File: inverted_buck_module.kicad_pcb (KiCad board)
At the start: 2 copper layers, 11 parts, among them J1 Conn_01x03, U1 TPS63710

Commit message: more wip
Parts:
- removed Cin1: 2x22uF 16V, Capacitor_SMD:C_0603_1608Metric
- removed Cout1: 2 x 22uF10V / 0805, Capacitor_SMD:C_0805_2012Metric
- removed Cx1: 2.2uF 16V 0603, Capacitor_SMD:C_0603_1608Metric
- removed R1: 130k, Resistor_SMD:R_0603_1608Metric
- removed R2: 24k, Resistor_SMD:R_0603_1608Metric
- added Ccp2: 10uF 16V, Capacitor_SMD:C_0805_2012Metric, F.Cu at (110.7, 61.8)
- added Ccp3: 10uF 16V, Capacitor_SMD:C_0805_2012Metric, F.Cu at (110.7, 59.8)
- added Cin: 22uF 16V, Capacitor_SMD:C_1206_3216Metric, F.Cu at (116.0, 56.5)
- added Cin2: 22uF 16V, Capacitor_SMD:C_1206_3216Metric, F.Cu at (118.5, 56.5)
- added Cin3: 22uF 16V, Capacitor_SMD:C_1206_3216Metric, F.Cu at (121.0, 56.5)
- added Cinx: 2.2uF 16V, Capacitor_SMD:C_0603_1608Metric, F.Cu at (114.0, 56.3)
- added Cout: 47uF 6.3V, Capacitor_SMD:C_0805_2012Metric, F.Cu at (102.7, 56.6)
- added Cout2: 47uF 6.3V, Capacitor_SMD:C_0805_2012Metric, F.Cu at (105.0, 56.5)
- added Cout3: 47uF 6.3V, Capacitor_SMD:C_0805_2012Metric, F.Cu at (107.5, 56.5)
- added Rfbb1: 24kΩ, Resistor_SMD:R_0402_1005Metric, F.Cu at (110.0, 52.0)
- added Rfbt1: 130kΩ, Resistor_SMD:R_0402_1005Metric, F.Cu at (110.0, 53.0)
- Caux: renamed from Caux1; value 220nF -> 220nF 10V
- Ccap1: value 1uF -> 1uF 10V
- Ccp: renamed from Ccp1; value 3 x 10uF 16V / 0805 -> 10uF 16V
- L1: value 4.7 uH -> 4.7uH; footprint Inductor_SMD:L_0603_1608Metric -> Inductor_SMD:L_Coilcraft_LPS4018
- moved L1 46.1 mm to (106.4, 60.6), turned to 180 degrees
- moved U1 45.1 mm to (110.7, 56.6), turned to -90 degrees
- moved J1 38.9 mm to (121.1, 65.0), turned to -90 degrees
- moved Ccap1 37.5 mm to (106.5, 52.3), turned to 90 degrees
- moved Caux 27.9 mm to (114.0, 52.3), turned to 90 degrees
- moved Ccp 26.4 mm to (110.7, 63.8), turned to 180 degrees
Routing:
- net GND: track 0.00 -> 39.1 mm, vias 0 -> 1
- net Vout: track 0.00 -> 35.5 mm
- net Vin: track 0.00 -> 21.7 mm, vias 0 -> 2
- net Net-(U1-SW): track 0.00 -> 7.80 mm
- net Net-(U1-CP): track 0.00 -> 5.89 mm
- net Net-(U1-CAP): track 0.00 -> 3.85 mm
- net Net-(U1-FB): track 0.00 -> 3.35 mm
- net Net-(U1-VAUX): track 0.00 -> 2.93 mm
- net Net-(U1-VREF): track 0.00 -> 2.16 mm
- added copper zone on B.Cu, net GND
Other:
- board outline added: 23 x 17.5 mm

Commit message: layout tweaks
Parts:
- moved Cin3 3.49 mm to (118.0, 54.7)
- moved Cin2 2.98 mm to (118.0, 59.5), turned to -90 degrees
- moved Caux 2.97 mm to (113.5, 55.2), turned to -90 degrees
- moved Cin 2.97 mm to (115.5, 59.5), turned to -90 degrees
- moved Cinx 2.48 mm to (113.5, 58.7), turned to -90 degrees
- moved Ccap1 1.02 mm to (107.5, 52.5), turned to 180 degrees
- moved Cout3 0.89 mm to (107.2, 55.7)
- moved Cout 0.88 mm to (102.8, 55.7)
- moved Ccp 0.84 mm to (110.8, 63.0)
- moved Cout2 0.83 mm to (105.0, 55.7)
- moved Ccp2 0.82 mm to (110.8, 61.0)
- moved Rfbt1 0.80 mm to (110.0, 52.2)
- moved Rfbb1 0.80 mm to (110.0, 51.2)
- moved Ccp3 0.79 mm to (110.8, 59.0)
- moved U1 0.78 mm to (110.7, 55.8)
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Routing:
- net GND: track 39.1 -> 16.3 mm, vias 1 -> 14
- net Vin: track 21.7 -> 27.2 mm, vias 2 -> 0
- net Net-(U1-VAUX): track 2.93 -> 1.55 mm
- net Net-(U1-CAP): track 3.85 -> 2.64 mm
- net Vout: track 35.5 -> 36.1 mm
- added copper zone on F.Cu, net GND
- added copper zone on F.Cu, net Vout

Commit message: fill areas
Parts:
- removed Ccap1: 1uF 10V, Capacitor_SMD:C_0603_1608Metric
- removed Rfbb1: 24kΩ, Resistor_SMD:R_0402_1005Metric
- removed Rfbt1: 130kΩ, Resistor_SMD:R_0402_1005Metric
- added Ccap: 1uF 10V, Capacitor_SMD:C_0603_1608Metric, F.Cu at (107.5, 52.5)
- added Rfbb: 24kΩ, Resistor_SMD:R_0402_1005Metric, F.Cu at (110.0, 51.5)
- added Rfbt: 130kΩ, Resistor_SMD:R_0402_1005Metric, F.Cu at (110.0, 52.5)
- J1: footprint Connector_PinHeader_2.54mm:PinHeader_1x03_P2.54mm_Horizontal -> Connector_PinHeader_2.54mm:PinHeader_1x03_P2.54mm_Vertical
- moved J1 1.58 mm to (119.5, 65.0)
- moved Cout 0.25 mm to (103.0, 55.7)
- moved Caux 0.20 mm to (113.5, 55.0)
- moved Cinx 0.20 mm to (113.5, 58.5)
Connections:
- net Net-(U1-CP) renamed /CP
- net Net-(U1-SW) renamed /SW
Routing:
- net GND: track 16.3 -> 14.1 mm
- net Vin: track 27.2 -> 29.2 mm
- net Vout: track 36.1 -> 35.4 mm
- added copper zone on F.Cu, net /CP
- added copper zone on F.Cu, net /SW
- added copper zone on F.Cu, net Vin
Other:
- board size 23 x 17.5 mm -> 21 x 17 mm

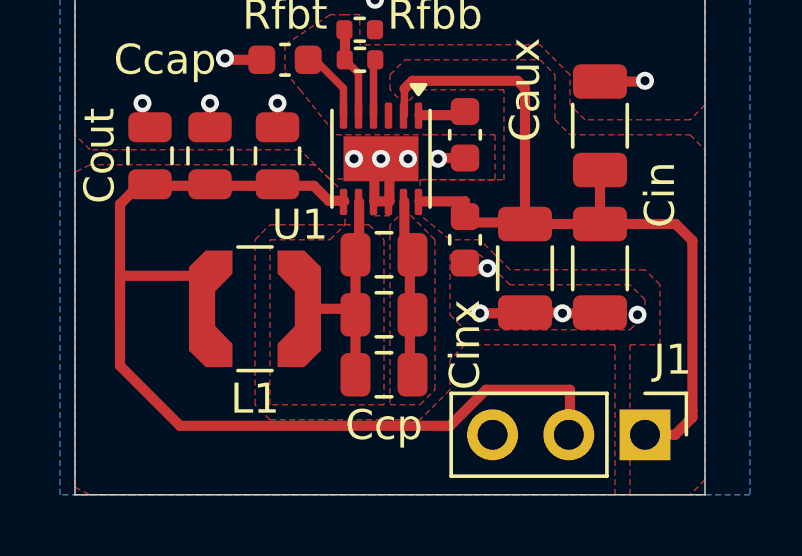
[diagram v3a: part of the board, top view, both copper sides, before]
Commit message: vout tweak
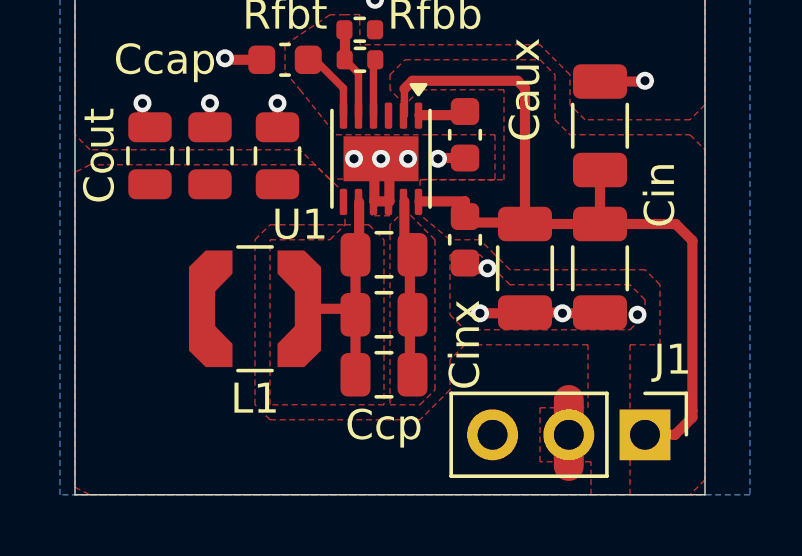
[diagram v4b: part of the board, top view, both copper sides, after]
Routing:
- net Vout: track 35.4 -> 2.26 mm
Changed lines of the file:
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@@
 	)
 	(segment
-		(start 114.2 63.5)
-		(end 117 63.5)
-		(width 0.34)
-		(layer "F.Cu")
-		(net 4)
-	)
-	(segment
-		(start 104.734998 59.7)
-		(end 104.735 59.700002)
-		(width 0.34)
-		(layer "F.Cu")
-		(net 4)
-	)
-	(segment
-		(start 113 64.7)
-		(end 114.2 63.5)
-		(width 0.34)
-		(layer "F.Cu")
-		(net 4)
-	)
-	(segment
-		(start 102.659598 56.7)
-		(end 102.636997 56.677399)
-		(width 0.34)
-		(layer "F.Cu")
-		(net 4)
-	)
-	(segment
-		(start 109.459623 57.2)
-		(end 108.959623 57.2)
-		(width 0.34)
-		(layer "F.Cu")
-		(net 4)
-	)
-	(segment
-		(start 109.480315 57.220692)
-		(end 109.459623 57.2)
-		(width 0.34)
-		(layer "F.Cu")
-		(net 4)
-	)
-	(segment
-		(start 102.636997 56.677399)
-		(end 102 57.314396)
-		(width 0.34)
-		(layer "F.Cu")
-		(net 4)
-	)
-	(segment
-		(start 108.459623 56.7)
-		(end 102.659598 56.7)
-		(width 0.34)
-		(layer "F.Cu")
-		(net 4)
-	)
-	(segment
-		(start 102 61.2)
-		(end 102 62.7)
-		(width 0.34)
-		(layer "F.Cu")
-		(net 4)
-	)
-	(segment
-		(start 108.959623 57.2)
-		(end 108.459623 56.7)
-		(width 0.34)
-		(layer "F.Cu")
-		(net 4)
-	)
-	(segment
-		(start 102 62.7)
-		(end 104 64.7)
-		(width 0.34)
-		(layer "F.Cu")
-		(net 4)
-	)
-	(segment
-		(start 102 61.2)
-		(end 102 59.7)
-		(width 0.34)
-		(layer "F.Cu")
-		(net 4)
-	)
-	(segment
-		(start 117 63.5)
-		(end 117 65)
-		(width 0.34)
-		(layer "F.Cu")
-		(net 4)
-	)
-	(segment
-		(start 102 59.7)
-		(end 104.734998 59.7)
-		(width 0.34)
-		(layer "F.Cu")
-		(net 4)
-	)
-	(segment
-		(start 104 64.7)
-		(end 113 64.7)
-		(width 0.34)
-		(layer "F.Cu")
-		(net 4)
-	)
-	(segment
-		(start 102 57.314396)
-		(end 102 61.2)
-		(width 0.34)
-		(layer "F.Cu")
-		(net 4)
-	)
-	(segment
-		(start 104.735 59.700002)
-		(end 104.735 59.7)
-		(width 0.34)
+		(start 116.96 65)
+		(end 116.96 63.84)
+		(width 1)
+		(layer "F.Cu")
+		(net 4)
+	)
+	(segment
+		(start 116.96 63.84)
+		(end 117 63.8)
+		(width 0.34)
+		(layer "F.Cu")
+		(net 4)
+	)
+	(segment
+		(start 116.96 65)
+		(end 116.96 66.04)
+		(width 1)
 		(layer "F.Cu")
 		(net 4)
@@
 		(polygon
 			(pts
-				(xy 106.5 58.5) (xy 107 58) (xy 109.5 58) (xy 109.5 58) (xy 109.5 56.975) (xy 109 56.475) (xy 108.5 56)
-				(xy 101 56) (xy 100.5 56.25) (xy 100.5 66.75) (xy 101 67) (xy 118.5 67) (xy 118.5 62) (xy 113.5 62)
-				(xy 113 62.5) (xy 113 63.5) (xy 112 64.5) (xy 107 64.5) (xy 106.5 64)
+				(xy 106.5 58.5) (xy 107 58) (xy 109.5 58) (xy 109.5 56.975) (xy 109 56.475) (xy 108.5 56) (xy 101 56)
+				(xy 100.5 56.25) (xy 100.5 66.75) (xy 101 67) (xy 117.7 67) (xy 117.7 65.9) (xy 116 65.9) (xy 116 64.1)
+				(xy 117.6 64.1) (xy 117.6 62) (xy 113.5 62) (xy 113 62.5) (xy 113 63.5) (xy 112 64.5) (xy 107 64.5)
+				(xy 106.5 64)
 			)
 		)

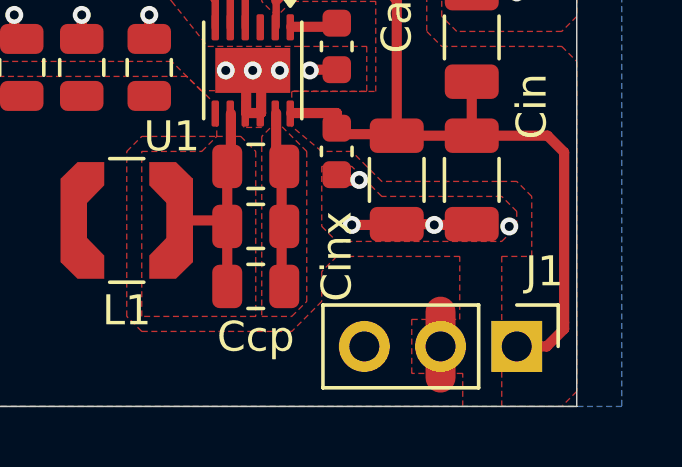
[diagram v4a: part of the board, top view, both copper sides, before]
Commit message: flip connector to the backside
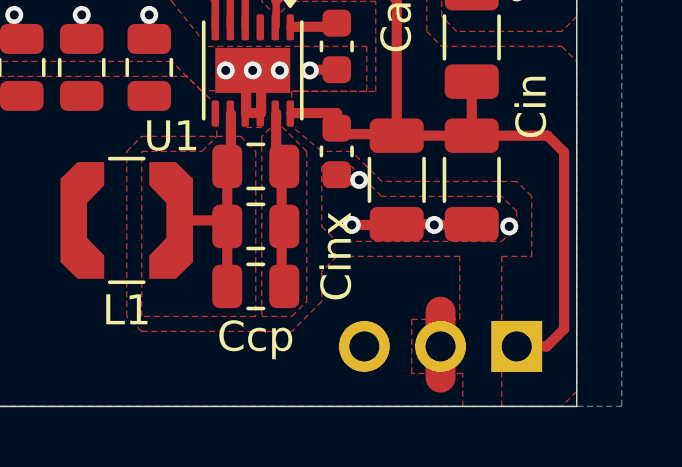
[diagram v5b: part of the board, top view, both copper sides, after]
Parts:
- J1: moved to B.Cu
- turned J1 to 90 degrees

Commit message: revert prop refs
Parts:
- renumbered Caux to Caux1, Ccap to Ccap1, Ccp to Ccp1, Cin to Cin1, Cinx to Cinx1, Cout to Cout1, Rfbb to Rfbb1, Rfbt to Rfbt1
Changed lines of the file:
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@@
 		(descr "Capacitor SMD 1206 (3216 Metric), square (rectangular) end terminal, IPC-7351 nominal, (Body size source: IPC-SM-782 page 76, https://www.pcb-3d.com/wordpress/wp-content/uploads/ipc-sm-782a_amendment_1_and_2.pdf), generated with kicad-footprint-generator")
 		(tags "capacitor")
-		(property "Reference" "Cin"
+		(property "Reference" "Cin1"
 			(at -2.45 -4.5 90)
 			(layer "F.SilkS")
@@
 		(descr "Capacitor SMD 0603 (1608 Metric), square (rectangular) end terminal, IPC-7351 nominal, (Body size source: IPC-SM-782 page 76, https://www.pcb-3d.com/wordpress/wp-content/uploads/ipc-sm-782a_amendment_1_and_2.pdf), generated with kicad-footprint-generator")
 		(tags "capacitor")
-		(property "Reference" "Ccap"
+		(property "Reference" "Ccap1"
 			(at 4 0 0)
 			(layer "F.SilkS")
@@
 		(descr "Resistor SMD 0402 (1005 Metric), square (rectangular) end terminal, IPC-7351 nominal, (Body size source: IPC-SM-782 page 72, https://www.pcb-3d.com/wordpress/wp-content/uploads/ipc-sm-782a_amendment_1_and_2.pdf), generated with kicad-footprint-generator")
 		(tags "resistor")
-		(property "Reference" "Rfbt"
+		(property "Reference" "Rfbt1"
 			(at 2.5 1.5 0)
 			(layer "F.SilkS")
@@
 		(descr "Capacitor SMD 0603 (1608 Metric), square (rectangular) end terminal, IPC-7351 nominal, (Body size source: IPC-SM-782 page 76, https://www.pcb-3d.com/wordpress/wp-content/uploads/ipc-sm-782a_amendment_1_and_2.pdf), generated with kicad-footprint-generator")
 		(tags "capacitor")
-		(property "Reference" "Caux"
+		(property "Reference" "Caux1"
 			(at -1.5 -2 90)
 			(layer "F.SilkS")
@@
 		(descr "Capacitor SMD 0805 (2012 Metric), square (rectangular) end terminal, IPC-7351 nominal, (Body size source: IPC-SM-782 page 76, https://www.pcb-3d.com/wordpress/wp-content/uploads/ipc-sm-782a_amendment_1_and_2.pdf, https://docs.google.com/spreadsheets/d/1BsfQQcO9C6DZCsRaXUlFlo91Tg2WpOkGARC1WS5S8t0/edit?usp=sharing), generated with kicad-footprint-generator")
 		(tags "capacitor")
-		(property "Reference" "Ccp"
+		(property "Reference" "Ccp1"
 			(at 0 -1.68 0)
 			(layer "F.SilkS")
@@
 		(descr "Resistor SMD 0402 (1005 Metric), square (rectangular) end terminal, IPC-7351 nominal, (Body size source: IPC-SM-782 page 72, https://www.pcb-3d.com/wordpress/wp-content/uploads/ipc-sm-782a_amendment_1_and_2.pdf), generated with kicad-footprint-generator")
 		(tags "resistor")
-		(property "Reference" "Rfbb"
+		(property "Reference" "Rfbb1"
 			(at 2.51 -0.5 0)
 			(layer "F.SilkS")
@@
 		(descr "Capacitor SMD 0805 (2012 Metric), square (rectangular) end terminal, IPC-7351 nominal, (Body size source: IPC-SM-782 page 76, https://www.pcb-3d.com/wordpress/wp-content/uploads/ipc-sm-782a_amendment_1_and_2.pdf, https://docs.google.com/spreadsheets/d/1BsfQQcO9C6DZCsRaXUlFlo91Tg2WpOkGARC1WS5S8t0/edit?usp=sharing), generated with kicad-footprint-generator")
 		(tags "capacitor")
-		(property "Reference" "Cout"
+		(property "Reference" "Cout1"
 			(at 0 -1.68 90)
 			(layer "F.SilkS")
@@
 		(descr "Capacitor SMD 0603 (1608 Metric), square (rectangular) end terminal, IPC-7351 nominal, (Body size source: IPC-SM-782 page 76, https://www.pcb-3d.com/wordpress/wp-content/uploads/ipc-sm-782a_amendment_1_and_2.pdf), generated with kicad-footprint-generator")
 		(tags "capacitor")
-		(property "Reference" "Cinx"
+		(property "Reference" "Cinx1"
 			(at 3.5 0 90)
 			(layer "F.SilkS")

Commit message: add lcsc parts
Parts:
- Rfbb1: value 24kΩ -> 24k
- Rfbt1: value 130kΩ -> 130k
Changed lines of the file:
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@@
 			)
 		)
+		(property "LCSC" "C385906"
+			(at 0 0 0)
+			(layer "F.SilkS")
+			(hide yes)
+			(effects
+				(font
+					(size 1.27 1.27)
+					(thickness 0.15)
+				)
+			)
+		)
 		(property ki_fp_filters "C_*")
 		(sheetname "/")
@@
 			)
 		)
+		(property "LCSC" "C385906"
+			(at 0 0 0)
+			(layer "F.SilkS")
+			(hide yes)
+			(effects
+				(font
+					(size 1.27 1.27)
+					(thickness 0.15)
+				)
+			)
+		)
 		(property ki_fp_filters "C_*")
 		(sheetname "/")
@@
 			)
 		)
+		(property "LCSC" "C19712575"
+			(at 0 0 0)
+			(layer "F.SilkS")
+			(hide yes)
+			(effects
+				(font
+					(size 1.27 1.27)
+					(thickness 0.15)
+				)
+			)
+		)
 		(property ki_fp_filters "Choke_* *Coil* Inductor_* L_*")
 		(sheetname "/")
@@
 			)
 		)
+		(property "LCSC" "C92806"
+			(at 0 0 0)
+			(layer "F.SilkS")
+			(hide yes)
+			(effects
+				(font
+					(size 1.27 1.27)
+					(thickness 0.15)
+				)
+			)
+		)
 		(property ki_fp_filters "C_*")
 		(sheetname "/")
@@
 			)
 		)
+		(property "LCSC" "C385906"
+			(at 0 0 0)
+			(layer "F.SilkS")
+			(hide yes)
+			(effects
+				(font
+					(size 1.27 1.27)
+					(thickness 0.15)
+				)
+			)
+		)
 		(property ki_fp_filters "C_*")
 		(sheetname "/")
@@
 			)
 		)
+		(property "LCSC" "C141287"
+			(at 0 0 0)
+			(layer "F.SilkS")
+			(hide yes)
+			(effects
+				(font
+					(size 1.27 1.27)
+					(thickness 0.15)
+				)
+			)
+		)
 		(property ki_fp_filters "C_*")
 		(sheetname "/")
@@
 			)
 		)
+		(property "LCSC" "C141287"
+			(at 0 0 0)
+			(layer "F.SilkS")
+			(hide yes)
+			(effects
+				(font
+					(size 1.27 1.27)
+					(thickness 0.15)
+				)
+			)
+		)
 		(property ki_fp_filters "C_*")
 		(sheetname "/")
@@
 			)
 		)
+		(property "LCSC" "C5785393"
+			(at 0 0 0)
+			(layer "F.SilkS")
+			(hide yes)
+			(effects
+				(font
+					(size 1.27 1.27)
+					(thickness 0.15)
+				)
+			)
+		)
 		(property ki_fp_filters "C_*")
 		(sheetname "/")
@@
 			)
 		)
-		(property "Value" "130kΩ"
+		(property "Value" "130k"
 			(at 0 1.17 0)
 			(layer "F.Fab")
@@
 			)
 		)
+		(property "LCSC" "C4352024"
+			(at 0 0 0)
+			(layer "F.SilkS")
+			(hide yes)
+			(effects
+				(font
+					(size 1.27 1.27)
+					(thickness 0.15)
+				)
+			)
+		)
 		(property ki_fp_filters "R_*")
 		(sheetname "/")
@@
 			)
 		)
+		(property "LCSC" "C5785393"
+			(at 0 0 0)
+			(layer "F.SilkS")
+			(hide yes)
+			(effects
+				(font
+					(size 1.27 1.27)
+					(thickness 0.15)
+				)
+			)
+		)
 		(property ki_fp_filters "C_*")
 		(sheetname "/")
@@
 			)
 		)
+		(property "LCSC" "C386049"
+			(at 0 0 0)
+			(layer "F.SilkS")
+			(hide yes)
+			(effects
+				(font
+					(size 1.27 1.27)
+					(thickness 0.15)
+				)
+			)
+		)
 		(property ki_fp_filters "C_*")
 		(sheetname "/")
@@
 			)
 		)
+		(property "LCSC" "C141287"
+			(at 0 0 0)
+			(layer "F.SilkS")
+			(hide yes)
+			(effects
+				(font
+					(size 1.27 1.27)
+					(thickness 0.15)
+				)
+			)
+		)
 		(property ki_fp_filters "C_*")
 		(sheetname "/")
@@
 			)
 		)
-		(property "Value" "24kΩ"
+		(property "Value" "24k"
 			(at 0 1.17 0)
 			(layer "F.Fab")
@@
 			)
 		)
+		(property "LCSC" "C2076708"
+			(at 0 0 0)
+			(layer "F.SilkS")
+			(hide yes)
+			(effects
+				(font
+					(size 1.27 1.27)
+					(thickness 0.15)
+				)
+			)
+		)
 		(property ki_fp_filters "R_*")
 		(sheetname "/")
@@
 			)
 		)
+		(property "LCSC" "C485552"
+			(at 0 0 0)
+			(layer "F.SilkS")
+			(hide yes)
+			(effects
+				(font
+					(size 1.27 1.27)
+					(thickness 0.15)
+				)
+			)
+		)
 		(sheetname "/")
 		(sheetfile "inverted_buck_module.kicad_sch")
@@
 			)
 		)
+		(property "LCSC" "C5785393"
+			(at 0 0 0)
+			(layer "F.SilkS")
+			(hide yes)
+			(effects
+				(font
+					(size 1.27 1.27)
+					(thickness 0.15)
+				)
+			)
+		)
 		(property ki_fp_filters "C_*")
 		(sheetname "/")
@@
 			)
 		)
+		(property "LCSC" "C337443"
+			(at 0 0 0)
+			(layer "F.SilkS")
+			(hide yes)
+			(effects
+				(font
+					(size 1.27 1.27)
+					(thickness 0.15)
+				)
+			)
+		)
 		(property ki_fp_filters "C_*")
 		(sheetname "/")
@@
 		(sheetname "/")
 		(sheetfile "inverted_buck_module.kicad_sch")
-		(attr through_hole)
+		(attr through_hole exclude_from_pos_files)
 		(fp_line
 			(start -1.38 -6.46)
